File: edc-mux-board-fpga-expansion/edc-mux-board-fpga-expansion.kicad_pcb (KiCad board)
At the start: 4 copper layers, 224.5 x 177.5 mm, 375 parts, among them J1 DC-62F, J2 Device 8, J3 Device 9, J4 Device 10, J5 Device 11, J6 Device 12, J7 Device 13, J8 Device 14, J9 Device 15, U1 EP5358HUI, U10 TLV320AIC3206, U11 FSA2367, U12 P82B96, U13 TLV320AIC3206, U14 FSA2367, U15 P82B96, U16 TLV320AIC3206, U17 FSA2367, U18 P82B96, U19 TLV320AIC3206, U2 R-78B3.3-2.0, U20 FSA2367, U21 P82B96, U22 TLV320AIC3206, U23 FSA2367, U24 P82B96, U25 TLV320AIC3206, U26 FSA2367, U27 CDCLVC1108, U28 TCA9555RTWR, U29 TCA9548A, U3 P82B96, U4 TLV320AIC3206, U5 FSA2367, U6 P82B96, U7 TLV320AIC3206, U8 FSA2367, U9 P82B96

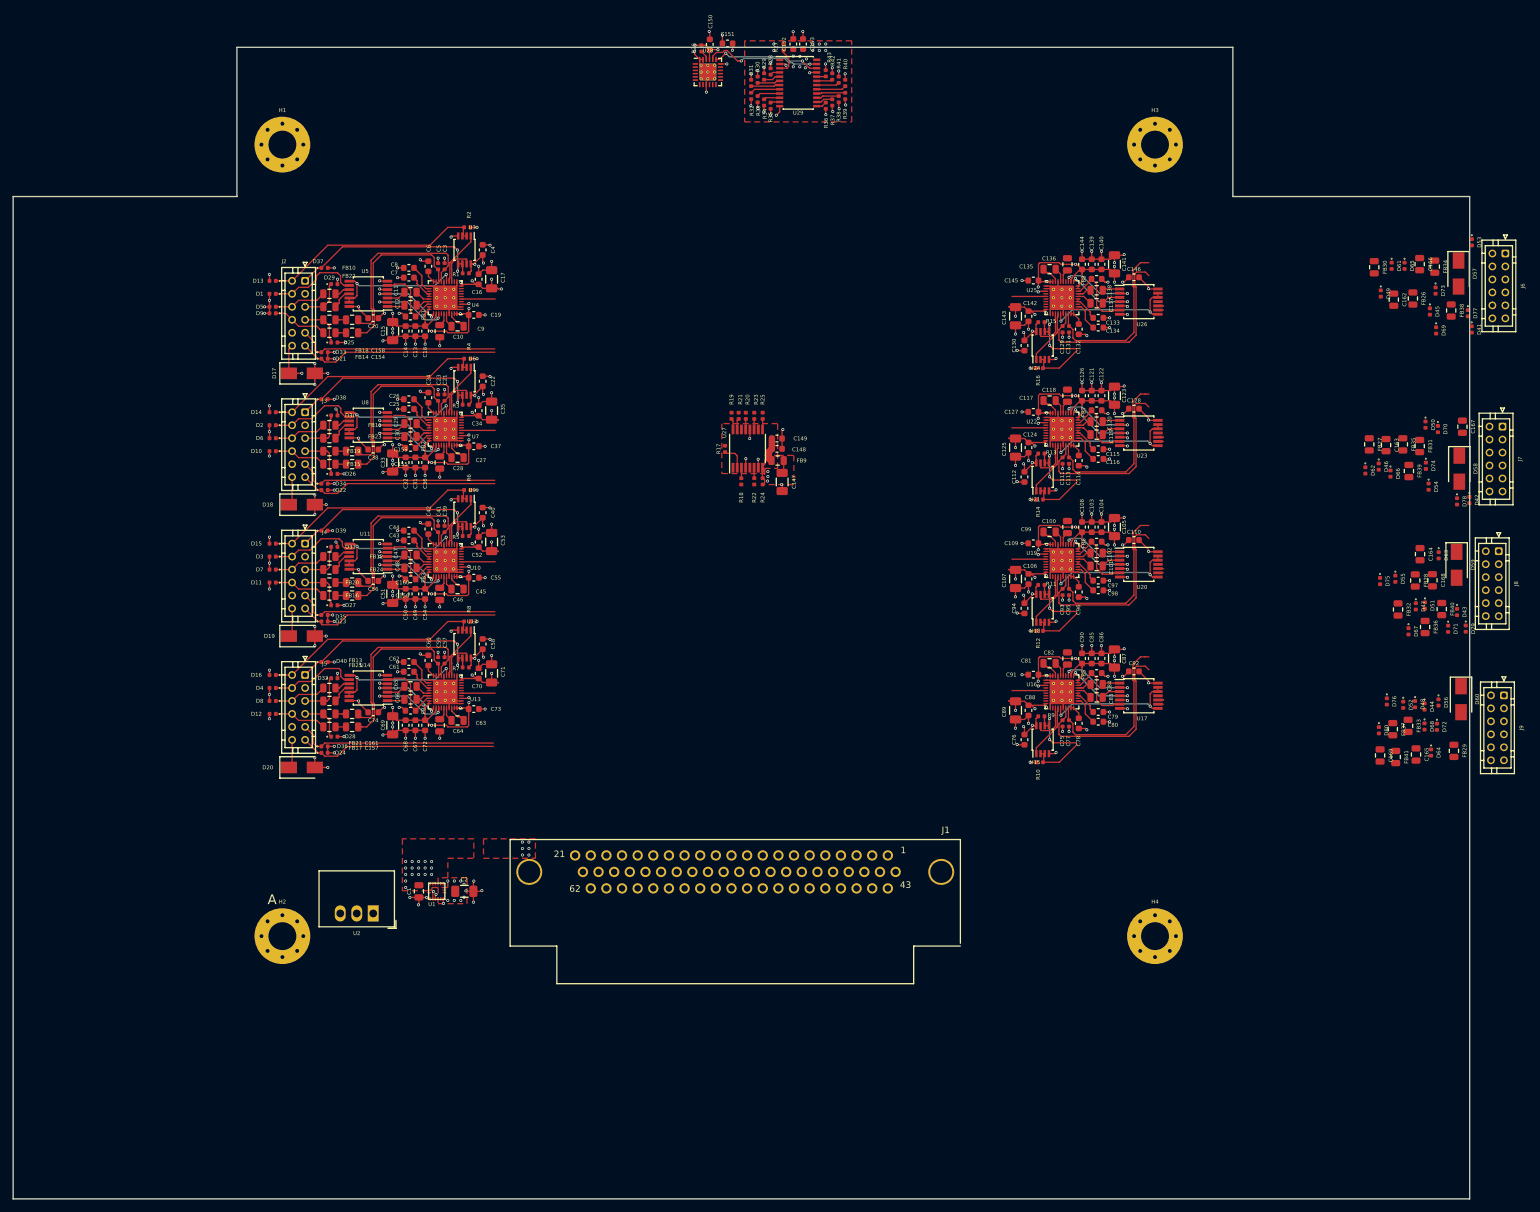
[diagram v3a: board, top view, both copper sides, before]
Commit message: Finished routing all 8 connector-codec pairs
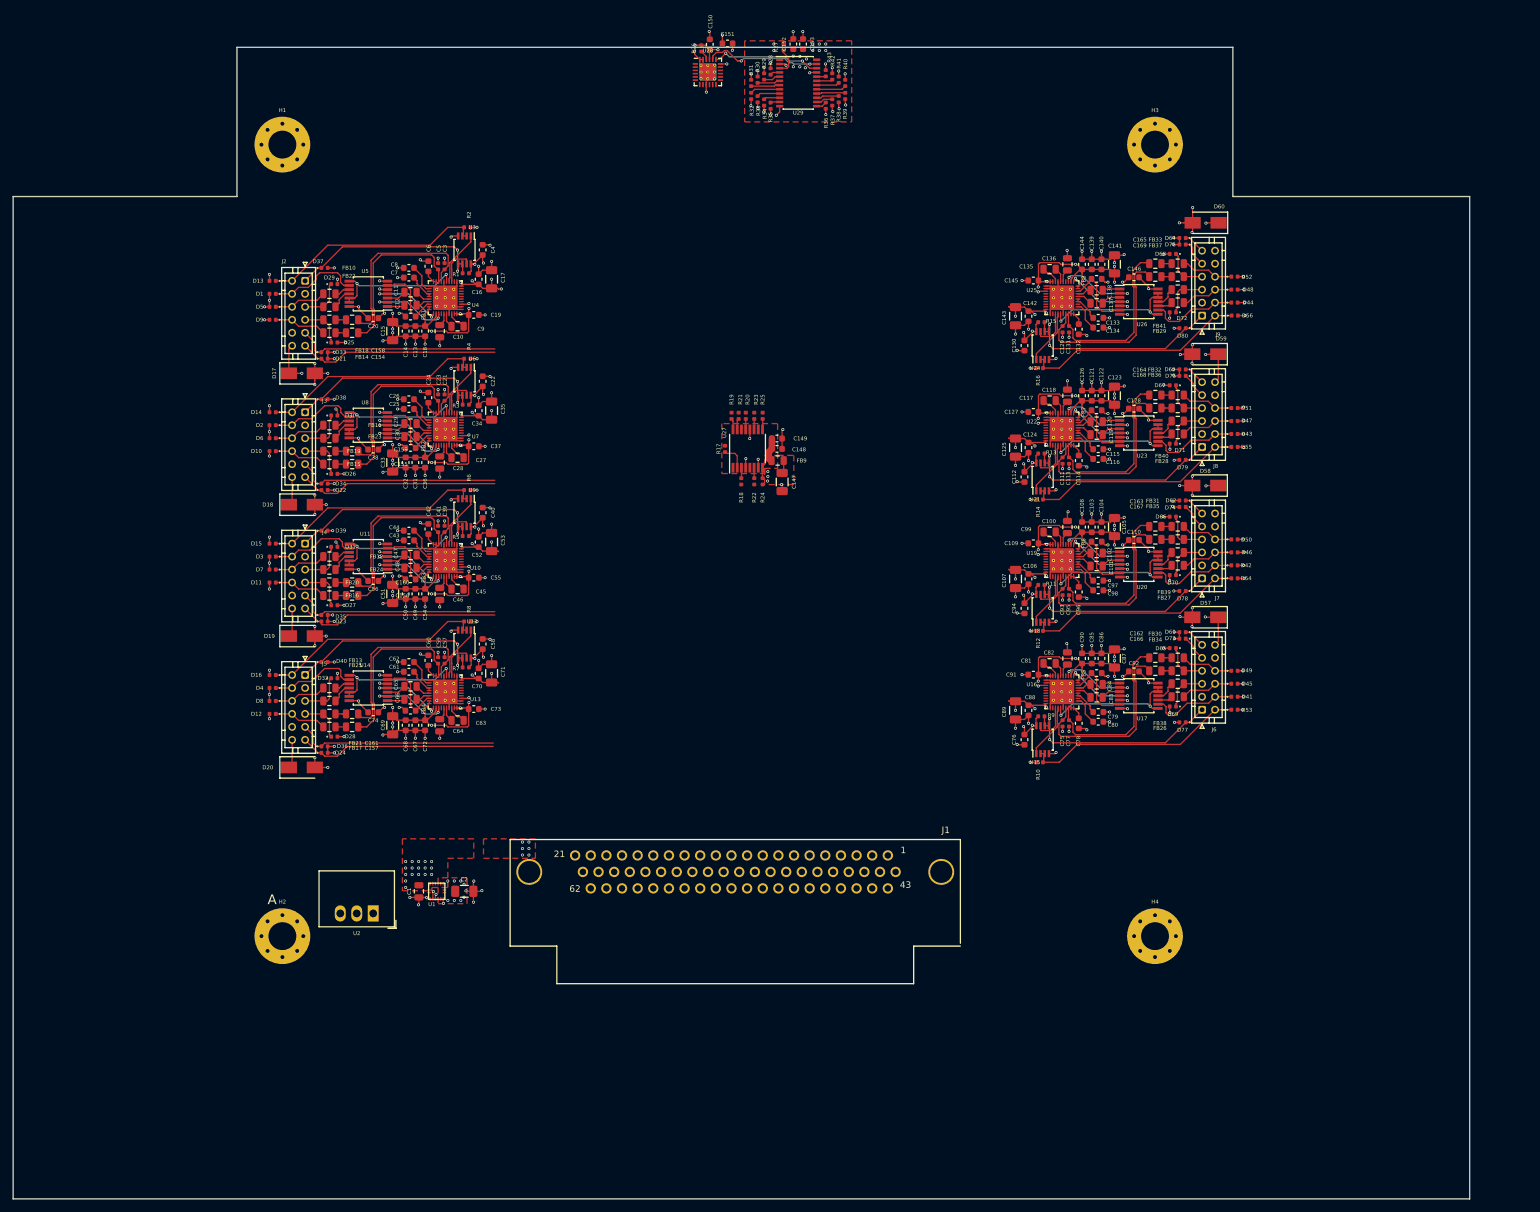
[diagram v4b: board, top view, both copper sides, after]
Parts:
- moved D64 88.1 mm to (244.2, 43.9), turned to 180 degrees
- moved C165 85.7 mm to (240.1, 47.9), turned to 180 degrees
- moved J6 84.4 mm to (247.2, 116.6), turned to 90 degrees
- moved D60 83.3 mm to (247.8, 41.5), turned to 180 degrees
- moved D68 82.5 mm to (242.8, 46.4), turned to 180 degrees
- moved C169 81.5 mm to (240.1, 49.9), turned to 0 degrees
- moved FB29 81.2 mm to (243.5, 53.9), turned to 180 degrees
- moved D53 80.8 mm to (252.2, 116.6), turned to 0 degrees
- moved FB33 79.6 mm to (243.5, 47.9), turned to 180 degrees
- moved FB41 79.5 mm to (243.5, 51.9), turned to 0 degrees
- moved FB37 77.2 mm to (243.5, 49.9), turned to 0 degrees
- moved D76 77.1 mm to (244.2, 44.9), turned to 180 degrees
- moved D77 76.9 mm to (244.2, 118.5), turned to 180 degrees
- moved D72 75.7 mm to (242.8, 55.4), turned to 180 degrees
- moved J9 74.8 mm to (247.2, 55.9), turned to 90 degrees
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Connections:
- J1 pad 1: Net-(J1-Pad1) -> /Bottom Side Connector Interconnects/DIN12
- J1 pad 10: Net-(J1-Pad10) -> (no net)
- J1 pad 11: Net-(J1-Pad11) -> (no net)
- J1 pad 12: Net-(J1-Pad12) -> (no net)
- J1 pad 13: Net-(J1-Pad13) -> (no net)
- J1 pad 14: Net-(J1-Pad14) -> /Bottom Side Connector Interconnects/DIN8
- J1 pad 15: Net-(J1-Pad15) -> /Bottom Side Connector Interconnects/BCLK8
- J1 pad 16: Net-(J1-Pad16) -> /Bottom Side Connector Interconnects/DIN9
- J1 pad 17: Net-(J1-Pad17) -> /Bottom Side Connector Interconnects/BCLK9
- J1 pad 18: Net-(J1-Pad18) -> /Bottom Side Connector Interconnects/DIN10
- J1 pad 19: Net-(J1-Pad19) -> /Bottom Side Connector Interconnects/BCLK10
- J1 pad 2: Net-(J1-Pad2) -> /Bottom Side Connector Interconnects/BCLK12
- J1 pad 20: Net-(J1-Pad20) -> /Bottom Side Connector Interconnects/DIN11
- J1 pad 21: Net-(J1-Pad21) -> /Bottom Side Connector Interconnects/BCLK11
- J1 pad 22: Net-(J1-Pad22) -> /Bottom Side Connector Interconnects/DOUT12
- J1 pad 23: Net-(J1-Pad23) -> /Bottom Side Connector Interconnects/WCLK12
- J1 pad 24: Net-(J1-Pad24) -> /Bottom Side Connector Interconnects/DOUT13
- J1 pad 25: Net-(J1-Pad25) -> /Bottom Side Connector Interconnects/WCLK13
- J1 pad 26: Net-(J1-Pad26) -> /Bottom Side Connector Interconnects/DOUT14
- J1 pad 27: Net-(J1-Pad27) -> /Bottom Side Connector Interconnects/WCLK14
- J1 pad 28: Net-(J1-Pad28) -> /Bottom Side Connector Interconnects/DOUT15
- J1 pad 29: Net-(J1-Pad29) -> /Bottom Side Connector Interconnects/WCLK15
- J1 pad 3: Net-(J1-Pad3) -> /Bottom Side Connector Interconnects/DIN13
- J1 pad 30: Net-(J1-Pad30) -> (no net)
- J1 pad 31: Net-(J1-Pad31) -> (no net)
- J1 pad 32: Net-(J1-Pad32) -> (no net)
- J1 pad 33: Net-(J1-Pad33) -> (no net)
- J1 pad 34: Net-(J1-Pad34) -> (no net)
- J1 pad 35: Net-(J1-Pad35) -> /Bottom Side Connector Interconnects/DOUT8
- J1 pad 36: Net-(J1-Pad36) -> /Bottom Side Connector Interconnects/WCLK8
- J1 pad 37: Net-(J1-Pad37) -> /Bottom Side Connector Interconnects/DOUT9
- J1 pad 38: Net-(J1-Pad38) -> /Bottom Side Connector Interconnects/WCLK9
- J1 pad 39: Net-(J1-Pad39) -> /Bottom Side Connector Interconnects/DOUT10
- J1 pad 4: Net-(J1-Pad4) -> /Bottom Side Connector Interconnects/BCLK13
- J1 pad 40: Net-(J1-Pad40) -> /Bottom Side Connector Interconnects/WCLK10
- J1 pad 41: Net-(J1-Pad41) -> /Bottom Side Connector Interconnects/DOUT11
- J1 pad 42: Net-(J1-Pad42) -> /Bottom Side Connector Interconnects/WCLK11
- J1 pad 43: Net-(J1-Pad43) -> (no net)
- J1 pad 44: Net-(J1-Pad44) -> (no net)
- J1 pad 45: Net-(J1-Pad45) -> (no net)
- J1 pad 46: Net-(J1-Pad46) -> (no net)
- J1 pad 47: Net-(J1-Pad47) -> (no net)
- J1 pad 48: Net-(J1-Pad48) -> (no net)
- J1 pad 49: Net-(J1-Pad49) -> (no net)
- J1 pad 5: Net-(J1-Pad5) -> /Bottom Side Connector Interconnects/DIN14
- J1 pad 50: Net-(J1-Pad50) -> (no net)
- J1 pad 51: Net-(J1-Pad51) -> (no net)
- J1 pad 52: Net-(J1-Pad52) -> (no net)
- J1 pad 53: Net-(J1-Pad53) -> (no net)
- J1 pad 54: Net-(J1-Pad54) -> (no net)
- J1 pad 55: Net-(J1-Pad55) -> (no net)
- J1 pad 56: Net-(J1-Pad56) -> (no net)
- J1 pad 57: Net-(J1-Pad57) -> (no net)
- J1 pad 58: Net-(J1-Pad58) -> (no net)
- J1 pad 59: Net-(J1-Pad59) -> (no net)
- J1 pad 6: Net-(J1-Pad6) -> /Bottom Side Connector Interconnects/BCLK14
- J1 pad 60: Net-(J1-Pad60) -> (no net)
- J1 pad 61: Net-(J1-Pad61) -> (no net)
- J1 pad 62: Net-(J1-Pad62) -> (no net)
- J1 pad 7: Net-(J1-Pad7) -> /Bottom Side Connector Interconnects/DIN15
- J1 pad 8: Net-(J1-Pad8) -> /Bottom Side Connector Interconnects/BCLK15
- J1 pad 9: Net-(J1-Pad9) -> (no net)
- U10 pad 6: (no net) -> /Bottom Side Connector Interconnects/BCLK10
- U10 pad 7: (no net) -> /Bottom Side Connector Interconnects/WCLK10
- U10 pad 8: (no net) -> /Bottom Side Connector Interconnects/DIN10
- U10 pad 9: (no net) -> /Bottom Side Connector Interconnects/DOUT10
- U13 pad 6: (no net) -> /Bottom Side Connector Interconnects/BCLK11
- U13 pad 7: (no net) -> /Bottom Side Connector Interconnects/WCLK11
- U13 pad 8: (no net) -> /Bottom Side Connector Interconnects/DIN11
- U13 pad 9: (no net) -> /Bottom Side Connector Interconnects/DOUT11
- U16 pad 6: (no net) -> /Bottom Side Connector Interconnects/BCLK12
- U16 pad 7: (no net) -> /Bottom Side Connector Interconnects/WCLK12
- U16 pad 8: (no net) -> /Bottom Side Connector Interconnects/DIN12
- U16 pad 9: (no net) -> /Bottom Side Connector Interconnects/DOUT12
- U19 pad 6: (no net) -> /Bottom Side Connector Interconnects/BCLK13
- U19 pad 7: (no net) -> /Bottom Side Connector Interconnects/WCLK13
- U19 pad 8: (no net) -> /Bottom Side Connector Interconnects/DIN13
- U19 pad 9: (no net) -> /Bottom Side Connector Interconnects/DOUT13
- U22 pad 6: (no net) -> /Bottom Side Connector Interconnects/BCLK14
- U22 pad 7: (no net) -> /Bottom Side Connector Interconnects/WCLK14
- U22 pad 8: (no net) -> /Bottom Side Connector Interconnects/DIN14
- U22 pad 9: (no net) -> /Bottom Side Connector Interconnects/DOUT14
- U25 pad 6: (no net) -> /Bottom Side Connector Interconnects/BCLK15
- U25 pad 7: (no net) -> /Bottom Side Connector Interconnects/WCLK15
- U25 pad 8: (no net) -> /Bottom Side Connector Interconnects/DIN15
- U25 pad 9: (no net) -> /Bottom Side Connector Interconnects/DOUT15
- U4 pad 6: (no net) -> /Bottom Side Connector Interconnects/BCLK8
- U4 pad 7: (no net) -> /Bottom Side Connector Interconnects/WCLK8
- U4 pad 8: (no net) -> /Bottom Side Connector Interconnects/DIN8
- U4 pad 9: (no net) -> /Bottom Side Connector Interconnects/DOUT8
- U7 pad 6: (no net) -> /Bottom Side Connector Interconnects/BCLK9
- U7 pad 7: (no net) -> /Bottom Side Connector Interconnects/WCLK9
- U7 pad 8: (no net) -> /Bottom Side Connector Interconnects/DIN9
- U7 pad 9: (no net) -> /Bottom Side Connector Interconnects/DOUT9
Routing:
- net GND: track 480.5 -> 541.9 mm, vias 230 -> 282
- net /CODEC interconnection sheet/SDA_HV15: track 8.33 -> 34.4 mm
- net /CODEC interconnection sheet/SDA_HV14: track 8.33 -> 34.3 mm
- net /CODEC interconnection sheet/SDA_HV13: track 8.33 -> 34.3 mm
- net /CODEC interconnection sheet/SDA_HV12: track 8.33 -> 34.3 mm
- net /CODEC interconnection sheet/SCL_HV13: track 10.9 -> 32.3 mm
- net /CODEC interconnection sheet/SCL_HV15: track 10.9 -> 32.3 mm
- net /CODEC interconnection sheet/SCL_HV14: track 10.9 -> 32.3 mm
- net /CODEC interconnection sheet/SCL_HV12: track 10.9 -> 32.3 mm
- net +12V: track 75.4 -> 92.3 mm, vias 25 -> 29
- net /CODEC interconnection sheet/AUD_GND12: track 0.85 -> 13.8 mm
- net /CODEC interconnection sheet/AUD_GND15: track 0.85 -> 13.8 mm
- net /CODEC interconnection sheet/AUD_GND13: track 0.85 -> 13.7 mm
- net /CODEC interconnection sheet/AUD_GND14: track 0.85 -> 13.7 mm
- net Net-(D51-Pad1): track 0.00 -> 8.16 mm
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
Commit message: positioned all codec-connector pairs and routed most clk and data lines
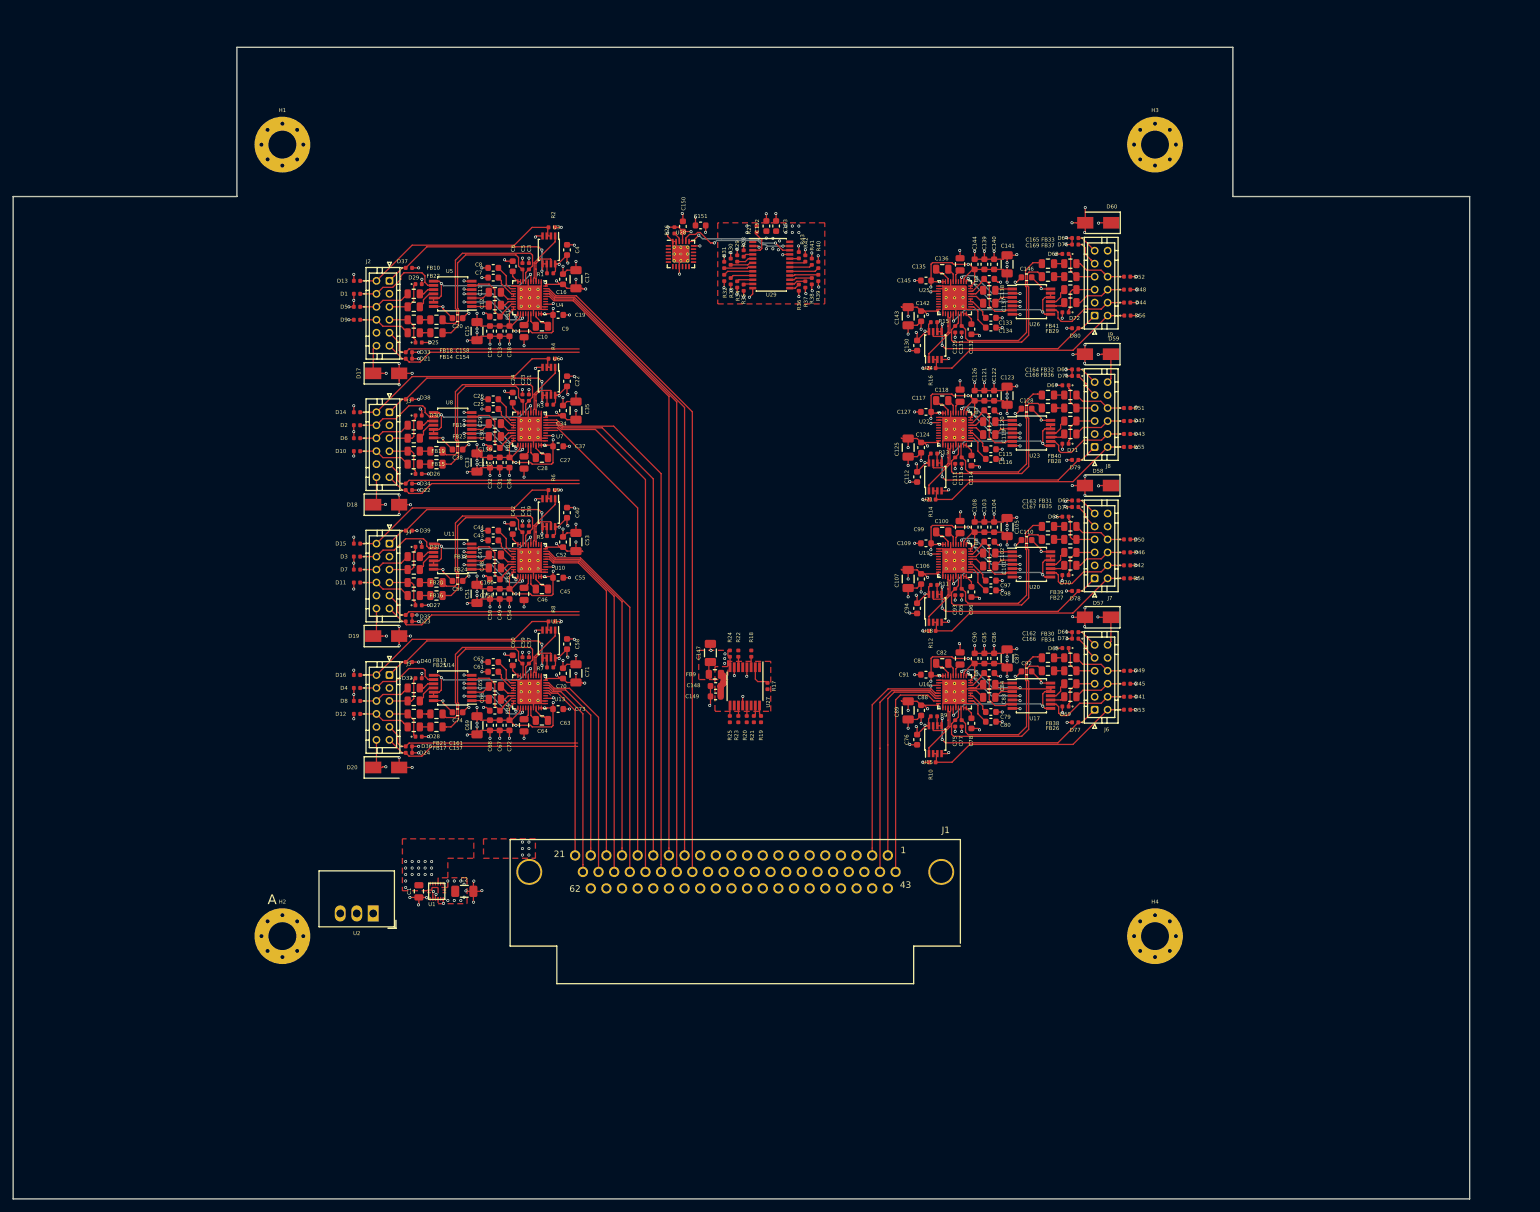
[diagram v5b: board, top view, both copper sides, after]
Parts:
- moved R25 47.0 mm to (174.5, 118.0), turned to 90 degrees
- moved R19 47.0 mm to (179.3, 118.0), turned to 90 degrees
- moved R23 46.8 mm to (175.8, 118.0), turned to 90 degrees
- moved R21 46.8 mm to (178.2, 118.0), turned to 90 degrees
- moved R20 46.8 mm to (177.1, 118.0), turned to 90 degrees
- moved C149 40.9 mm to (172.3, 114.5), turned to 180 degrees
- moved C148 37.8 mm to (172.3, 113.0), turned to 0 degrees
- moved R17 37.1 mm to (180.3, 113.0), turned to 270 degrees
- moved U27 36.7 mm to (176.8, 113.0), turned to 270 degrees
- moved FB9 34.3 mm to (172.2, 111.2), turned to 180 degrees
- moved C147 28.6 mm to (171.5, 107.8), turned to 90 degrees
- moved C151 28.4 mm to (170.0, 42.0)
- moved R26 28.4 mm to (165.9, 42.7)
- moved R28 28.4 mm to (176.6, 46.3)
- moved U28 28.4 mm to (166.9, 46.4)
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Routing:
- net /Bottom Side Connector Interconnects/DOUT8: track 0.00 -> 101.4 mm
- net /Bottom Side Connector Interconnects/WCLK8: track 0.00 -> 99.5 mm
- net /Bottom Side Connector Interconnects/DIN8: track 0.00 -> 97.9 mm
- net /Bottom Side Connector Interconnects/BCLK8: track 0.00 -> 96.1 mm
- net /Bottom Side Connector Interconnects/DOUT9: track 0.00 -> 82.6 mm
- net /Bottom Side Connector Interconnects/WCLK9: track 0.00 -> 79.3 mm
- net /Bottom Side Connector Interconnects/DIN9: track 0.00 -> 78.2 mm
- net /Bottom Side Connector Interconnects/BCLK9: track 0.00 -> 72.9 mm
- net /Bottom Side Connector Interconnects/DOUT10: track 0.00 -> 57.3 mm
- net /Bottom Side Connector Interconnects/WCLK10: track 0.00 -> 55.6 mm
- net /Bottom Side Connector Interconnects/DIN10: track 0.00 -> 53.9 mm
- net /Bottom Side Connector Interconnects/BCLK10: track 0.00 -> 52.2 mm
- net /Bottom Side Connector Interconnects/WCLK12: track 0.00 -> 36.3 mm
- net /Bottom Side Connector Interconnects/BCLK12: track 0.00 -> 34.7 mm
- net /Bottom Side Connector Interconnects/DOUT11: track 0.00 -> 34.2 mm
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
